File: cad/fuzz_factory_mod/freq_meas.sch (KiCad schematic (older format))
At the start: 16 parts

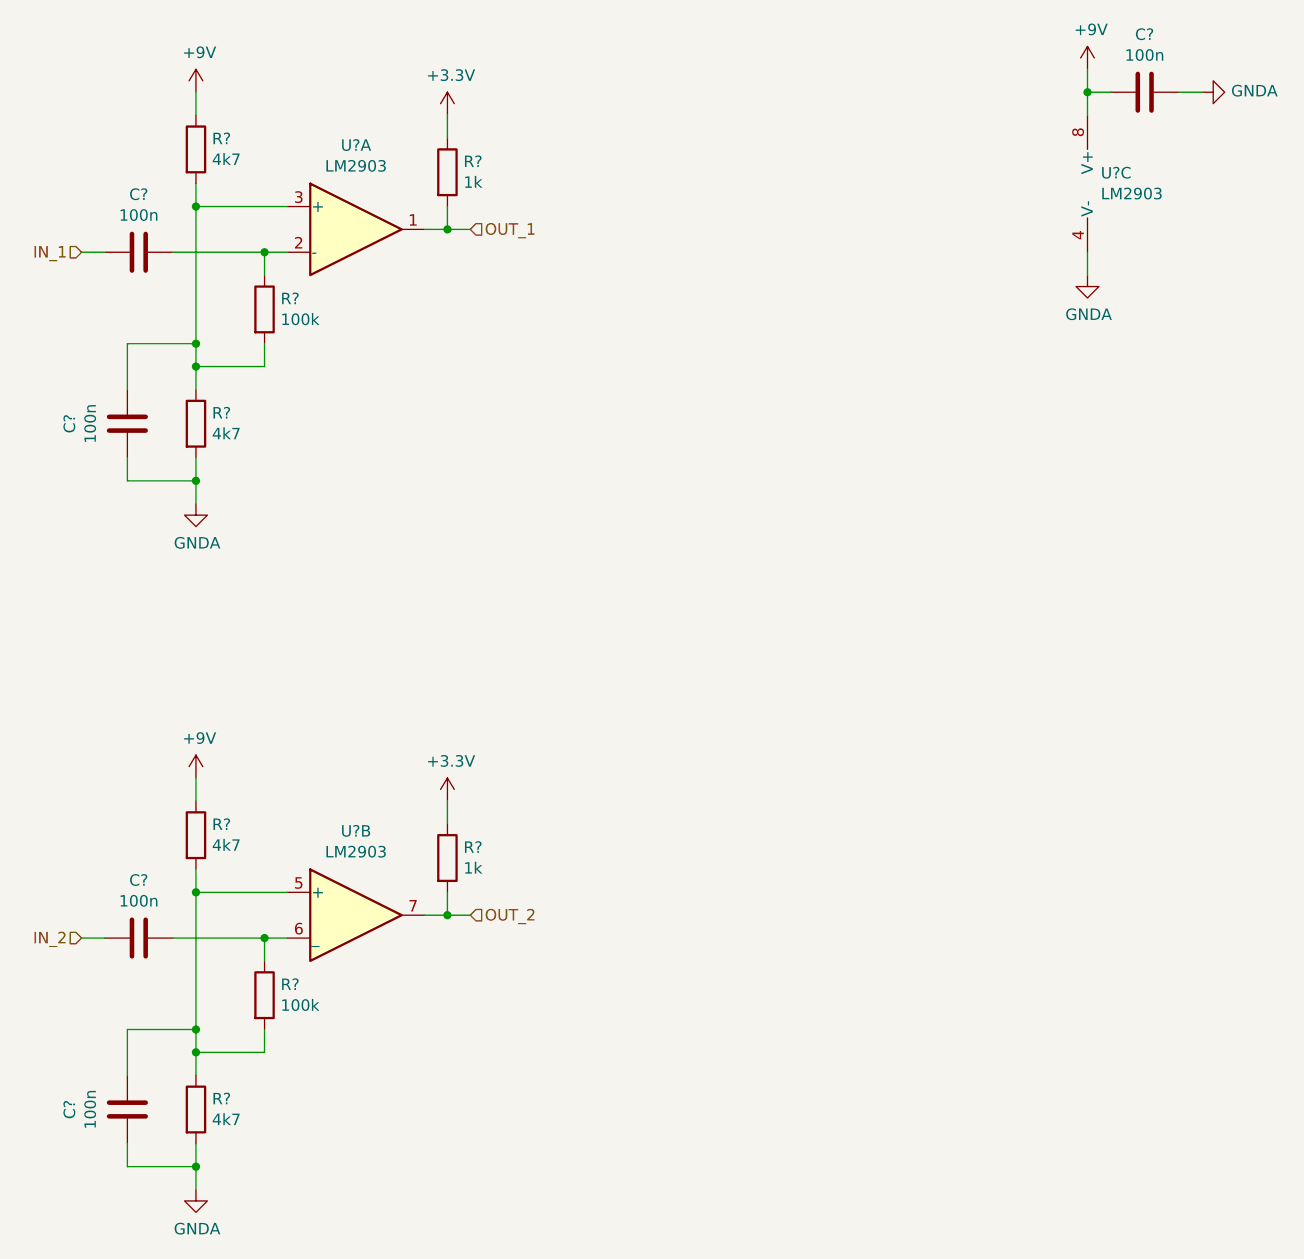
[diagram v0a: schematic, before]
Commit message: Continued schematic.
Modified fuuz_factory circuit : use of matched transistor pairs.
Added USB interface, through FT230X and direct to MCU.
Associated footprints, except for XTAL and trimmers.
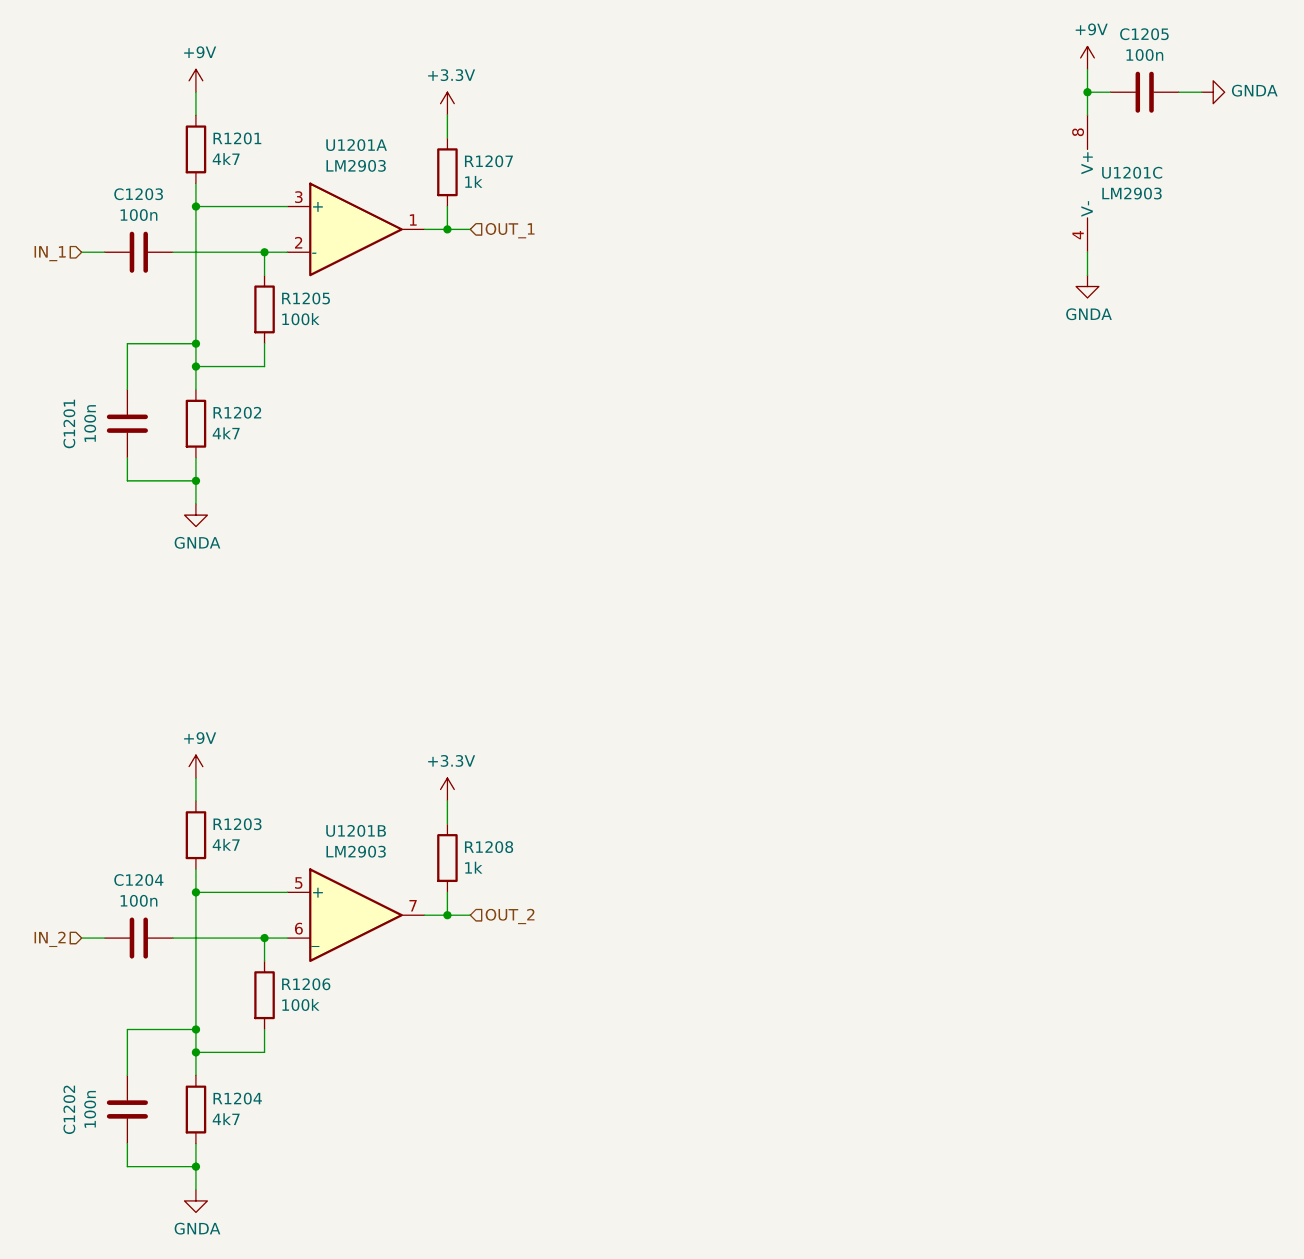
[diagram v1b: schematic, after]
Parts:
- C1201, C1202, C1203, C1204, C1205: renamed from C?; footprint (none) -> Capacitors_SMD:C_0603
- R1201, R1202, R1203, R1204, R1205, R1206, R1207, R1208: renamed from R?; footprint (none) -> Resistors_SMD:R_0603
- U1201: renamed from U?; footprint (none) -> Housings_SOIC:SOIC-8_3.9x4.9mm_Pitch1.27mm
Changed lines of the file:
@@
 $Descr A4 11693 8268
 encoding utf-8
-Sheet 10 19
+Sheet 12 22
 Title ""
 Date ""
@@
 $EndDescr
 $Comp
-L Comparator:LM2903 U?
+L Comparator:LM2903 U1201
 U 1 1 5E6C0D90
 P 2800 2100
-F 0 "U?" H 2800 2467 50  0000 C CNN
+F 0 "U1201" H 2800 2467 50  0000 C CNN
 F 1 "LM2903" H 2800 2376 50  0000 C CNN
-F 2 "" H 2800 2100 50  0001 C CNN
+F 2 "Housings_SOIC:SOIC-8_3.9x4.9mm_Pitch1.27mm" H 2800 2100 50  0001 C CNN
 F 3 "http://www.ti.com/lit/ds/symlink/lm393-n.pdf" H 2800 2100 50  0001 C CNN
 	1    2800 2100
@@
 $EndComp
 $Comp
-L Comparator:LM2903 U?
+L Comparator:LM2903 U1201
 U 3 1 5E6C2373
 P 6100 1900
-F 0 "U?" H 6058 1946 50  0000 L CNN
+F 0 "U1201" H 6058 1946 50  0000 L CNN
 F 1 "LM2903" H 6058 1855 50  0000 L CNN
-F 2 "" H 6100 1900 50  0001 C CNN
+F 2 "Housings_SOIC:SOIC-8_3.9x4.9mm_Pitch1.27mm" H 6100 1900 50  0001 C CNN
 F 3 "http://www.ti.com/lit/ds/symlink/lm393-n.pdf" H 6100 1900 50  0001 C CNN
 	3    6100 1900
@@
 $EndComp
 $Comp
-L Device:R R?
+L Device:R R1207
 U 1 1 5E6C3BDB
 P 3200 1850
-F 0 "R?" H 3270 1896 50  0000 L CNN
+F 0 "R1207" H 3270 1896 50  0000 L CNN
 F 1 "1k" H 3270 1805 50  0000 L CNN
-F 2 "" V 3130 1850 50  0001 C CNN
+F 2 "Resistors_SMD:R_0603" V 3130 1850 50  0001 C CNN
 F 3 "~" H 3200 1850 50  0001 C CNN
 	1    3200 1850
@@
 $EndComp
 $Comp
-L Device:R R?
+L Device:R R1205
 U 1 1 5E6C4D6C
 P 2400 2450
-F 0 "R?" H 2470 2496 50  0000 L CNN
+F 0 "R1205" H 2470 2496 50  0000 L CNN
 F 1 "100k" H 2470 2405 50  0000 L CNN
-F 2 "" V 2330 2450 50  0001 C CNN
+F 2 "Resistors_SMD:R_0603" V 2330 2450 50  0001 C CNN
 F 3 "~" H 2400 2450 50  0001 C CNN
 	1    2400 2450
@@
 $EndComp
 $Comp
-L Device:R R?
+L Device:R R1201
 U 1 1 5E6C5E4F
 P 2100 1750
-F 0 "R?" H 2170 1796 50  0000 L CNN
+F 0 "R1201" H 2170 1796 50  0000 L CNN
 F 1 "4k7" H 2170 1705 50  0000 L CNN
-F 2 "" V 2030 1750 50  0001 C CNN
+F 2 "Resistors_SMD:R_0603" V 2030 1750 50  0001 C CNN
 F 3 "~" H 2100 1750 50  0001 C CNN
 	1    2100 1750
@@
 $EndComp
 $Comp
-L Device:R R?
+L Device:R R1202
 U 1 1 5E6C6A5E
 P 2100 2950
-F 0 "R?" H 2170 2996 50  0000 L CNN
+F 0 "R1202" H 2170 2996 50  0000 L CNN
 F 1 "4k7" H 2170 2905 50  0000 L CNN
-F 2 "" V 2030 2950 50  0001 C CNN
+F 2 "Resistors_SMD:R_0603" V 2030 2950 50  0001 C CNN
 F 3 "~" H 2100 2950 50  0001 C CNN
 	1    2100 2950
@@
 $EndComp
 $Comp
-L power:GNDA #PWR?
+L power:GNDA #PWR01202
 U 1 1 5E6C7645
 P 2100 3300
-F 0 "#PWR?" H 2100 3050 50  0001 C CNN
+F 0 "#PWR01202" H 2100 3050 50  0001 C CNN
 F 1 "GNDA" H 2105 3127 50  0000 C CNN
 F 2 "" H 2100 3300 50  0001 C CNN
@@
 	3200 2100 3100 2100
 $Comp
-L power:+9V #PWR?
+L power:+9V #PWR01207
 U 1 1 5E6CBDCF
 P 6000 1400
-F 0 "#PWR?" H 6000 1250 50  0001 C CNN
+F 0 "#PWR01207" H 6000 1250 50  0001 C CNN
 F 1 "+9V" H 6015 1573 50  0000 C CNN
 F 2 "" H 6000 1400 50  0001 C CNN
@@
 $EndComp
 $Comp
-L power:GNDA #PWR?
+L power:GNDA #PWR01208
 U 1 1 5E6CD11C
 P 6000 2300
-F 0 "#PWR?" H 6000 2050 50  0001 C CNN
+F 0 "#PWR01208" H 6000 2050 50  0001 C CNN
 F 1 "GNDA" H 6005 2127 50  0000 C CNN
 F 2 "" H 6000 2300 50  0001 C CNN
@@
 	6000 1400 6000 1500
 $Comp
-L Device:C C?
+L Device:C C1205
 U 1 1 5E6CDEE4
 P 6250 1500
-F 0 "C?" V 5998 1500 50  0000 C CNN
+F 0 "C1205" V 5998 1500 50  0000 C CNN
 F 1 "100n" V 6089 1500 50  0000 C CNN
-F 2 "" H 6288 1350 50  0001 C CNN
+F 2 "Capacitors_SMD:C_0603" H 6288 1350 50  0001 C CNN
 F 3 "~" H 6250 1500 50  0001 C CNN
 	1    6250 1500
@@
 	6000 1500 6000 1600
 $Comp
-L power:GNDA #PWR?
+L power:GNDA #PWR01209
 U 1 1 5E6CECB1
 P 6500 1500
-F 0 "#PWR?" H 6500 1250 50  0001 C CNN
+F 0 "#PWR01209" H 6500 1250 50  0001 C CNN
 F 1 "GNDA" V 6505 1372 50  0000 R CNN
 F 2 "" H 6500 1500 50  0001 C CNN
@@
 	6500 1500 6400 1500
 $Comp
-L Device:C C?
+L Device:C C1203
 U 1 1 5E6CF778
 P 1850 2200
-F 0 "C?" V 1598 2200 50  0000 C CNN
+F 0 "C1203" V 1598 2200 50  0000 C CNN
 F 1 "100n" V 1689 2200 50  0000 C CNN
-F 2 "" H 1888 2050 50  0001 C CNN
+F 2 "Capacitors_SMD:C_0603" H 1888 2050 50  0001 C CNN
 F 3 "~" H 1850 2200 50  0001 C CNN
 	1    1850 2200
@@
 	2400 2200 2000 2200
 $Comp
-L power:+9V #PWR?
+L power:+9V #PWR01201
 U 1 1 5E6D0A58
 P 2100 1500
-F 0 "#PWR?" H 2100 1350 50  0001 C CNN
+F 0 "#PWR01201" H 2100 1350 50  0001 C CNN
 F 1 "+9V" H 2115 1673 50  0000 C CNN
 F 2 "" H 2100 1500 50  0001 C CNN
@@
 	3200 1600 3200 1700
 $Comp
-L power:+3.3V #PWR?
+L power:+3.3V #PWR01205
 U 1 1 5E6D62D7
 P 3200 1600
-F 0 "#PWR?" H 3200 1450 50  0001 C CNN
+F 0 "#PWR01205" H 3200 1450 50  0001 C CNN
 F 1 "+3.3V" H 3215 1773 50  0000 C CNN
 F 2 "" H 3200 1600 50  0001 C CNN
@@
 Connection ~ 3200 2100
 $Comp
-L Comparator:LM2903 U?
+L Comparator:LM2903 U1201
 U 2 1 5E6DA4DB
 P 2800 5100
-F 0 "U?" H 2800 5467 50  0000 C CNN
+F 0 "U1201" H 2800 5467 50  0000 C CNN
 F 1 "LM2903" H 2800 5376 50  0000 C CNN
-F 2 "" H 2800 5100 50  0001 C CNN
+F 2 "Housings_SOIC:SOIC-8_3.9x4.9mm_Pitch1.27mm" H 2800 5100 50  0001 C CNN
 F 3 "http://www.ti.com/lit/ds/symlink/lm393-n.pdf" H 2800 5100 50  0001 C CNN
 	2    2800 5100
@@
 $EndComp
 $Comp
-L Device:R R?
+L Device:R R1208
 U 1 1 5E6DA4E5
 P 3200 4850
-F 0 "R?" H 3270 4896 50  0000 L CNN
+F 0 "R1208" H 3270 4896 50  0000 L CNN
 F 1 "1k" H 3270 4805 50  0000 L CNN
-F 2 "" V 3130 4850 50  0001 C CNN
+F 2 "Resistors_SMD:R_0603" V 3130 4850 50  0001 C CNN
 F 3 "~" H 3200 4850 50  0001 C CNN
 	1    3200 4850
@@
 $EndComp
 $Comp
-L Device:R R?
+L Device:R R1206
 U 1 1 5E6DA4EF
 P 2400 5450
-F 0 "R?" H 2470 5496 50  0000 L CNN
+F 0 "R1206" H 2470 5496 50  0000 L CNN
 F 1 "100k" H 2470 5405 50  0000 L CNN
-F 2 "" V 2330 5450 50  0001 C CNN
+F 2 "Resistors_SMD:R_0603" V 2330 5450 50  0001 C CNN
 F 3 "~" H 2400 5450 50  0001 C CNN
 	1    2400 5450
@@
 $EndComp
 $Comp
-L Device:R R?
+L Device:R R1203
 U 1 1 5E6DA4F9
 P 2100 4750
-F 0 "R?" H 2170 4796 50  0000 L CNN
+F 0 "R1203" H 2170 4796 50  0000 L CNN
 F 1 "4k7" H 2170 4705 50  0000 L CNN
-F 2 "" V 2030 4750 50  0001 C CNN
+F 2 "Resistors_SMD:R_0603" V 2030 4750 50  0001 C CNN
 F 3 "~" H 2100 4750 50  0001 C CNN
 	1    2100 4750
@@
 $EndComp
 $Comp
-L Device:R R?
+L Device:R R1204
 U 1 1 5E6DA503
 P 2100 5950
-F 0 "R?" H 2170 5996 50  0000 L CNN
+F 0 "R1204" H 2170 5996 50  0000 L CNN
 F 1 "4k7" H 2170 5905 50  0000 L CNN
-F 2 "" V 2030 5950 50  0001 C CNN
+F 2 "Resistors_SMD:R_0603" V 2030 5950 50  0001 C CNN
 F 3 "~" H 2100 5950 50  0001 C CNN
 	1    2100 5950
@@
 $EndComp
 $Comp
-L power:GNDA #PWR?
+L power:GNDA #PWR01204
 U 1 1 5E6DA50D
 P 2100 6300
-F 0 "#PWR?" H 2100 6050 50  0001 C CNN
+F 0 "#PWR01204" H 2100 6050 50  0001 C CNN
 F 1 "GNDA" H 2105 6127 50  0000 C CNN
 F 2 "" H 2100 6300 50  0001 C CNN
@@
 	3200 5100 3100 5100
 $Comp
-L Device:C C?
+L Device:C C1204
 U 1 1 5E6DA522
 P 1850 5200
-F 0 "C?" V 1598 5200 50  0000 C CNN
+F 0 "C1204" V 1598 5200 50  0000 C CNN
 F 1 "100n" V 1689 5200 50  0000 C CNN
-F 2 "" H 1888 5050 50  0001 C CNN
+F 2 "Capacitors_SMD:C_0603" H 1888 5050 50  0001 C CNN
 F 3 "~" H 1850 5200 50  0001 C CNN
 	1    1850 5200
@@
 	2400 5200 2000 5200
 $Comp
-L power:+9V #PWR?
+L power:+9V #PWR01203
 U 1 1 5E6DA530
 P 2100 4500
-F 0 "#PWR?" H 2100 4350 50  0001 C CNN
+F 0 "#PWR01203" H 2100 4350 50  0001 C CNN
 F 1 "+9V" H 2115 4673 50  0000 C CNN
 F 2 "" H 2100 4500 50  0001 C CNN
@@
 	3200 4600 3200 4700
 $Comp
-L power:+3.3V #PWR?
+L power:+3.3V #PWR01206
 U 1 1 5E6DA53C
 P 3200 4600
-F 0 "#PWR?" H 3200 4450 50  0001 C CNN
+F 0 "#PWR01206" H 3200 4450 50  0001 C CNN
 F 1 "+3.3V" H 3215 4773 50  0000 C CNN
 F 2 "" H 3200 4600 50  0001 C CNN
@@
 Connection ~ 3200 5100
 $Comp
-L Device:C C?
+L Device:C C1201
 U 1 1 5E6F2DED
 P 1800 2950
-F 0 "C?" V 1548 2950 50  0000 C CNN
+F 0 "C1201" V 1548 2950 50  0000 C CNN
 F 1 "100n" V 1639 2950 50  0000 C CNN
-F 2 "" H 1838 2800 50  0001 C CNN
+F 2 "Capacitors_SMD:C_0603" H 1838 2800 50  0001 C CNN
 F 3 "~" H 1800 2950 50  0001 C CNN
 	1    1800 2950
@@
 	2100 6100 2100 6200
 $Comp
-L Device:C C?
+L Device:C C1202
 U 1 1 5E6F6E56
 P 1800 5950
-F 0 "C?" V 1548 5950 50  0000 C CNN
+F 0 "C1202" V 1548 5950 50  0000 C CNN
 F 1 "100n" V 1639 5950 50  0000 C CNN
-F 2 "" H 1838 5800 50  0001 C CNN
+F 2 "Capacitors_SMD:C_0603" H 1838 5800 50  0001 C CNN
 F 3 "~" H 1800 5950 50  0001 C CNN
 	1    1800 5950
